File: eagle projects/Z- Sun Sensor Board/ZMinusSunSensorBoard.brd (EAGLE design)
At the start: 91 x 91 mm, 194 parts, among them J2 HIROSE_FH19C-6S-0.5SH(10), J3 HIROSE_FH19C-6S-0.5SH(10), J4 HIROSE_FH19C-6S-0.5SH(10), J5 HIROSE_FH19C-6S-0.5SH(10), U1 ADS7841E_2K5, U13 ADS7841E_2K5, U15 TLV9051IDCKR, U19 TLV9051IDCKR, U2 ADS7841E_2K5, U21 TLV9051IDCKR, U23 TLV9051IDCKR, U24 TLV9051IDCKR, U25 ADS7841E_2K5, U26 TLV9051IDCKR, U27 ADS7841E_2K5, U28 TLV9051IDCKR, U29 TLV9051IDCKR, U3 TLV9051IDCKR, U30 TLV9051IDCKR, U31 TLV9051IDCKR, U32 TLV9051IDCKR, U4 LM20BIM7X_NOPB, U6 TLV9051IDCKR, U8 TLV9051IDCKR, U9 TLV9051IDCKR

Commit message: Rev B almost ready
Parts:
- removed A1: XY_SUN_SENSOR, my_library:XY_SUN_SENOR_MASK
- removed C104, C107, C109, C112, C114, C31, C69, C86, C97: 0.1u, resistor:C0402
- removed C105, C110, C111, C115, C116, C33, C54, C70, C84, C98: 0.022u, resistor:C0402
- removed C106, C108, C113, C55, C68, C85, C99: 4.7u, resistor:C0402
- removed C30: 4.7u, rcl:C0805
- removed J4, J5: HIROSE_FH19C-6S-0.5SH(10), my_library:HIROSE_FH19C-6S-0.5SH(10)
- removed JP1: (no value), pinhead:1X02
- removed JP3: (no value), pinhead:2X05
- removed R2: 0R, rcl:R0805
- removed R28, R57, R63, R69: 13.7k, resistor:R0402
- removed R31, R46, R55, R61, R67: 3.74k, resistor:R0402
- removed R56, R62, R68: 280R, resistor:R0402
- removed TP12, TP18, TP20, TP7, TP8: TESTPOINT, my_library:TP_P76H50
- removed U15, U24, U28, U30, U31, U32: TLV9051IDCKR, my_library:SC70-5P65_210X110L36X22N_TLV9051
- added C10, C17, C24, C36, C39, C4, C58, C64, C7: 0.1u, resistor:C0402
- added C11, C18, C34, C37, C40, C5, C59, C8: 0.022u, resistor:C0402
- added C13, C23, C3, C35, C38, C44, C57, C6, C63, C9: 4.7u, rcl:C0805
- added C2: 0.1u, rcl:C0402
- added J1: TE-1734829-2, my_library:TE-1734829-2
- added JP2, JP4, JP5, JP6: (no value), my_library:1X06_MTG_HOLES
- added R27: 5.1M, rcl:R0402
- added R30, R37, R43, R49, R71, R79: 280R, resistor:R0402
- added R35, R41, R72, R74, R80: 13.7k, resistor:R0402
- added R36, R42, R73, R75, R81: 3.74k, resistor:R0402
- added TP23, TP24, TP25, TP27, TP29: TESTPOINT, my_library:TP_P76H50
- added U$1: SSR_MOUNT_03, my_library:SSR_MOUNT_03
- added U$3, U$4, U$5: (no value), my_library:PHOTODIODE_SILK
- added U10, U11, U12, U14, U16, U17: TSV991AILT, my_library:SOT95P280X145-5N
- added U5: LM20BIM7X_NOPB, my_library:SOT23-5P65_210X110L40X22N_LM20
- C100, C71: value 0.022u -> 4.7u; device resistor:C0402 -> rcl:C0805
- C101, C27, C32: value 0.022u -> 0.1u
- C103, C96: value 4.7u -> 0.022u
- C25, C28: value 4.7u -> 0.022u; device rcl:C0805 -> resistor:C0402
- C26, C29: value 0.1u -> 4.7u; device resistor:C0402 -> rcl:C0805
- C52, C82: value 4.7u -> 0.1u
- C53, C67, C83: value 0.1u -> 0.022u
- C87: device resistor:C0402 -> rcl:C0805
- J2: value HIROSE_FH19C-6S-0.5SH(10) -> (none); device my_library:HIROSE_FH19C-6S-0.5SH(10) -> my_library:2X05
- J3: value HIROSE_FH19C-6S-0.5SH(10) -> (none); device my_library:HIROSE_FH19C-6S-0.5SH(10) -> my_library:1X02
- LED1: device led:CHIP-LED0603 -> led:CHIPLED-0603-TTW
- R14, R25: value 280R -> 5.1M; device resistor:R0402 -> rcl:R0402
- R15: value 13.7k -> 5.1M; device resistor:R0402 -> rcl:R0402
- R17: device resistor:R0402 -> rcl:R0402
- R19: value 3.74k -> 5.1M; device resistor:R0402 -> rcl:R0402
- R44, R53, R59, R65: value 280R -> 13.7k
- R45, R54, R60, R66: value 13.7k -> 3.74k
- R58, R64, R70: value 3.74k -> 280R
- U19, U21, U23, U26, U29, U3, U6, U8, U9: value TLV9051IDCKR -> TSV991AILT; device my_library:SC70-5P65_210X110L36X22N_TLV9051 -> my_library:SOT95P280X145-5N
- moved R21 134.9 mm to (87.0, 73.0), flipped to the bottom
- moved R18 127.5 mm to (87.0, 67.9), flipped to the bottom
- moved R17 125.3 mm to (87.0, 70.5), flipped to the bottom
- moved R12 121.4 mm to (87.0, 74.3), flipped to the bottom
- moved R16 121.4 mm to (87.0, 69.2), flipped to the bottom
- moved J2 78.7 mm to (81.3, 69.2)
- moved C50 76.5 mm to (71.8, 88.6), turned to 180 degrees
- moved C49 75.0 mm to (71.8, 87.3), turned to 180 degrees
- moved J3 75.0 mm to (14.0, 71.4), turned to 180 degrees
- moved LED1 70.7 mm to (15.2, 75.6)
- moved R11 70.6 mm to (13.3, 75.6)
- moved C46 70.3 mm to (65.1, 87.3), turned to 180 degrees
- moved R60 69.2 mm to (77.5, 29.2), turned to 90 degrees
- moved U13 68.4 mm to (68.6, 83.8), turned to 180 degrees
- moved C45 68.4 mm to (61.9, 87.3), turned to 0 degrees
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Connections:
- removed net !CS!_SUN_Z+: U2.15
- removed net N$1: R2.1, U4.3
- removed net N$13: R14.2, R15.1, U9.1
- removed net N$3: A1.C1, C27.1, R7.1, U6.3
- removed net N$31: R22.2, R23.1, U3.1
- removed net N$34: R25.2, R28.1, U23.1
- removed net N$36: R32.2, R33.1, U24.1
- removed net N$45: R44.2, R45.1, U19.1
- removed net N$47: R50.2, R51.1, U21.1
- removed net N$48: LED1.A, R11.1
- removed net N$5: TP17.1, U25.2
- removed net N$56: R56.2, R57.1, U28.1
- removed net N$58: R59.2, R60.1, U29.1
- removed net N$64: R65.2, R66.1, U31.1
- removed net N$66: R68.2, R69.1, U32.1
- removed net N$68: JP3.10
- removed net N$9: R8.2, R9.1, U8.1
- removed net TEMP: R2.2, TP1.1, U2.2
- new net N$20: R27.1, U5.1
- new net N$21: LED1.A@1, R11.1
- new net N$27: C8.1, R13.1, U$1.C2, U8.4
- new net N$28: R8.2, R9.1, U8.3
- new net N$30: R43.2, R44.1, U12.3
- new net N$32: R22.2, R23.1, U3.3
- new net N$40: R30.2, R35.1, U9.3
- new net N$42: C18.1, R42.1, U$1.C1, U11.4
- new net N$43: R37.2, R41.1, U11.3
- new net N$60: R49.2, R53.1, U14.3
- new net N$69: R64.2, R65.1, U23.3
- new net N$71: R71.2, R72.1, U17.3
- new net N$74: R70.2, R74.1, U26.3
- new net N$78: R79.2, R80.1, U29.3
- new net TEMP_EXT: TP17.1, U25.2, U5.3
- new net TEMP_INT: TP1.1, U2.2, U4.3
- net !CS!_SUN_X+: now also J2.2; no longer JP3.2
- net !CS!_SUN_X-: now also J2.7; no longer JP3.7
- net !CS!_SUN_Y+: now also J2.4; no longer JP3.4
- net !CS!_SUN_Y-: now also J2.9; no longer JP3.9
- net !CS!_SUN_Z-: now also J2.6, U2.15; no longer JP3.6
- net +3V3: now also C10.1, C100.1, C101.1, C13.1, C17.1, C2.1, C23.1, C24.1, C27.1, C3.1, C32.1, C35.1, C36.1, C38.1, C39.1, C4.1, C44.1, C57.1, C58.1, C6.1, C63.1, C64.1, C7.1, C71.1, C9.1, J1.1, J2.10, J3.1, R35.2, R41.2, R44.2, R53.2, R59.2, R65.2, R72.2, R74.2, R80.2, U10.5, U11.5, U12.5, U14.5, U16.5, U17.5, U5.4; no longer C103.1, C104.1, C106.1, C107.1, C108.1, C109.1, C112.1, C113.1, C114.1, C25.1, C28.1, C30.1, C31.1, C53.1, C55.1, C67.1, C68.1, C69.1, C83.1, C85.1, C86.1, C96.1, C97.1, C99.1, JP1.1, R15.2, R28.2, R45.2, R54.2, R57.2, R60.2, R63.2, R66.2, R69.2, U15.5, U24.5, U28.5, U30.5, U31.5, U32.5
- net 0_DEGREES: now also C18.2, R42.2, TP24.1, U11.1; no longer C27.2, R7.2, TP3.1, U6.4
- net 120_DEGREES: now also C8.2, U8.1; no longer C32.2, U8.4
- net 240_DEGREES: now also C5.2, R7.2, TP3.1, U6.1; no longer C33.2, R19.2, TP8.1, U9.4
- net GND: now also C10.2, C100.2, C101.2, C13.2, C17.2, C2.2, C23.2, C24.2, C27.2, C3.2, C32.2, C35.2, C36.2, C38.2, C39.2, C4.2, C44.2, C57.2, C58.2, C6.2, C63.2, C64.2, C7.2, C71.2, C9.2, J1.2, JP2.2, JP2.4, JP2.6, JP4.2, JP4.4, JP4.6, JP5.2, JP5.4, JP5.6, JP6.2, JP6.4, JP6.6, LED1.C@1, R15.1, R19.1, R25.2, R27.2, R30.1, R37.1, R43.1, R49.1, R58.1, R64.1, R70.1, R71.1, R79.1, U$1.A1, U$1.A2, U$1.A3, U10.2, U11.2, U12.2, U14.2, U16.2, U17.2, U5.2, U5.5; no longer A1.A1, A1.A2, A1.A3, C103.2, C104.2, C106.2, C107.2, C108.2, C109.2, C112.2, C113.2, C114.2, C25.2, C28.2, C30.2, C31.2, C53.2, C55.2, C67.2, C68.2, C69.2, C83.2, C85.2, C86.2, C96.2, C97.2, C99.2, J2.2, J2.4, J2.6, J2.7, J2.8, J3.4, J3.6, J3.7, J3.8, J4.2, J4.4, J4.6, J4.7, J4.8, J5.2, J5.4, J5.6, J5.7, J5.8, JP1.2, LED1.C, R25.1, R44.1, R53.1, R56.1, R59.1, R62.1, R65.1, R68.1, U15.2, U24.2, U28.2, U30.2, U31.2, U32.2
- net N$10: now also R15.2
- net N$11: now also R14.2
- net N$12: now also C5.1, R7.1, U$1.C3, U6.4; no longer A1.C3, C33.1, R19.1, U9.3
- net N$14: now also R19.2
- net N$23: now also C96.1, JP6.3, R75.1, U26.4; no longer C100.1, J5.3, R31.1, U23.3
- net N$29: now also C83.1, JP6.1, R66.1, U23.4; no longer C84.1, J5.1, R24.1, U3.3
- net N$35: now also C103.1, JP6.5, R81.1, U29.4; no longer C101.1, J5.5, R34.1, U24.3
- net N$37: now also C34.1, JP5.1, R45.1, U12.4; no longer C98.1, J4.1, R64.1, U30.3
- net N$38: now also C25.1, JP4.1, U10.4; no longer C54.1, J3.1, U15.3
- net N$41: now also R32.2, R33.1, U16.3; no longer R38.2, R39.1, U15.1
- net N$44: now also C40.1, JP4.3, R24.1, U3.4; no longer C70.1, J3.3, R46.1, U19.3
- net N$46: now also C53.1, JP4.5, R34.1, U16.4; no longer C71.1, J3.5, R52.1, U21.3
- net N$49: now also C11.1, JP2.1, R36.1, U9.4; no longer C105.1, J2.1, R55.1, U26.3
- net N$54: now also R50.2, R51.1, U19.3; no longer R53.2, R54.1, U26.1
- net N$55: now also C28.1, JP2.3, R54.1, U14.4; no longer C110.1, J2.3, R58.1, U28.3
- net N$57: now also C37.1, JP2.5, R73.1, U17.4; no longer C111.1, J2.5, R61.1, U29.3
- net N$6: now also R38.2, R39.1, U10.3; no longer R1.2, R3.1, U6.1
- net N$61: now also R58.2, R59.1, U21.3; no longer R62.2, R63.1, U30.1
- net N$63: now also C59.1, JP5.3, R52.1, U19.4; no longer C115.1, J4.3, R67.1, U31.3
- net N$65: now also C67.1, JP5.5, R60.1, U21.4; no longer C116.1, J4.5, R70.1, U32.3
- net N$67: now also J2.8, R25.1; no longer JP3.8
- net N$8: now also R1.2, R3.1, U6.3; no longer A1.C2, C32.1, R13.1, U8.3
- net UCB0_SPI_CLK: now also J2.5; no longer JP3.5
- net UCB0_SPI_MISO: now also J2.1; no longer JP3.1
- net UCB0_SPI_MOSI: now also J2.3; no longer JP3.3
- net X+_0_DEGREES: now also C11.2, R36.2, U9.1; no longer C105.2, R55.2, U26.4
- net X+_120_DEGREES: now also C28.2, R54.2, TP16.1, U14.1; no longer C110.2, R58.2, TP15.1, U28.4
- net X+_240_DEGREES: now also C37.2, R73.2, TP25.1, U17.1; no longer C111.2, R61.2, TP16.1, U29.4
- net X-_0_DEGREES: now also C25.2, U10.1; no longer C54.2, U15.4
- net X-_120_DEGREES: now also C40.2, R24.2, TP5.1, U3.1; no longer C70.2, R46.2, TP11.1, U19.4
- net X-_240_DEGREES: now also C53.2, R34.2, TP9.1, U16.1; no longer C71.2, R52.2, TP12.1, U21.4
- net Y+_0_DEGREES: now also C34.2, R45.2, TP11.1, U12.1; no longer C98.2, R64.2, TP18.1, U30.4
- net Y+_120_DEGREES: now also C59.2, R52.2, TP15.1, U19.1; no longer C115.2, R67.2, TP19.1, U31.4
- net Y+_240_DEGREES: now also C67.2, R60.2, TP19.1, U21.1; no longer C116.2, R70.2, TP20.1, U32.4
- net Y-_0_DEGREES: now also C103.2, R81.2, TP29.1, U29.1; no longer C84.2, R24.2, TP5.1, U3.4
- net Y-_120_DEGREES: now also C96.2, R75.2, TP27.1, U26.1; no longer C100.2, R31.2, TP7.1, U23.4
- net Y-_240_DEGREES: now also C83.2, R66.2, TP23.1, U23.1; no longer C101.2, R34.2, TP9.1, U24.4
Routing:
- net +3V3: track 149.7 -> 488.3 mm, vias 42 -> 53
- net UCB0_SPI_CLK: track 6.65 -> 67.4 mm, vias 4 -> 0
- net UCB0_SPI_MISO: track 1.89 -> 60.6 mm, vias 1 -> 9
- net TEMP_EXT: track 0.00 -> 40.7 mm, vias 0 -> 1
- net N$3: track 35.5 -> 0.00 mm
- net N$52: track 0.00 -> 27.5 mm, vias 0 -> 2
- net !CS!_SUN_Y+: track 0.00 -> 26.0 mm, vias 0 -> 2
- net TEMP: track 21.9 -> 0.00 mm
- net N$50: track 0.00 -> 21.4 mm, vias 0 -> 2
- net N$51: track 0.00 -> 21.4 mm, vias 0 -> 2
- net N$14: track 2.34 -> 23.2 mm, vias 0 -> 4
- net TEMP_INT: track 0.00 -> 20.1 mm
- net N$27: track 0.00 -> 18.0 mm, vias 1 -> 0
- net 0_DEGREES: track 28.5 -> 45.9 mm
- net 240_DEGREES: track 22.2 -> 39.4 mm
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- added copper zone on layer 15, net +3V10
- added copper zone on layer 15, net +3V11
- added copper zone on layer 15, net +3V12
- added copper zone on layer 15, net +3V14
- added copper zone on layer 15, net +3V16
- added copper zone on layer 15, net +3V18
- added copper zone on layer 15, net +3V20
- added copper zone on layer 15, net +3V22
- added copper zone on layer 15, net +3V24
- added copper zone on layer 15, net +3V4
- added copper zone on layer 15, net +3V5
- added copper zone on layer 15, net +3V6
- added copper zone on layer 15, net +3V7
- added copper zone on layer 15, net +3V8
- added copper zone on layer 15, net +3V9
- added copper zone on layer 2, net GND10
- added copper zone on layer 2, net GND11
- added copper zone on layer 2, net GND13
- added copper zone on layer 2, net GND15
- added copper zone on layer 2, net GND17
- added copper zone on layer 2, net GND19
- added copper zone on layer 2, net GND21
- added copper zone on layer 2, net GND23
- added copper zone on layer 2, net GND3
- added copper zone on layer 2, net GND4
- added copper zone on layer 2, net GND5
- added copper zone on layer 2, net GND6
- added copper zone on layer 2, net GND7
- added copper zone on layer 2, net GND8
- added copper zone on layer 2, net GND9
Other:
- outline, holes or cut-outs redrawn
- board text removed: "U15"
- board text removed: "U19"
- board text removed: "U21"
- board text removed: "U23"
- board text removed: "U24"
- board text removed: "U26"
- board text removed: "U28"
- board text removed: "U29"
- board text removed: "U30"
- board text removed: "U31"
- board text removed: "U32"
- board text removed: "U6"
- board text removed: "U8"
- board text removed: "U9"

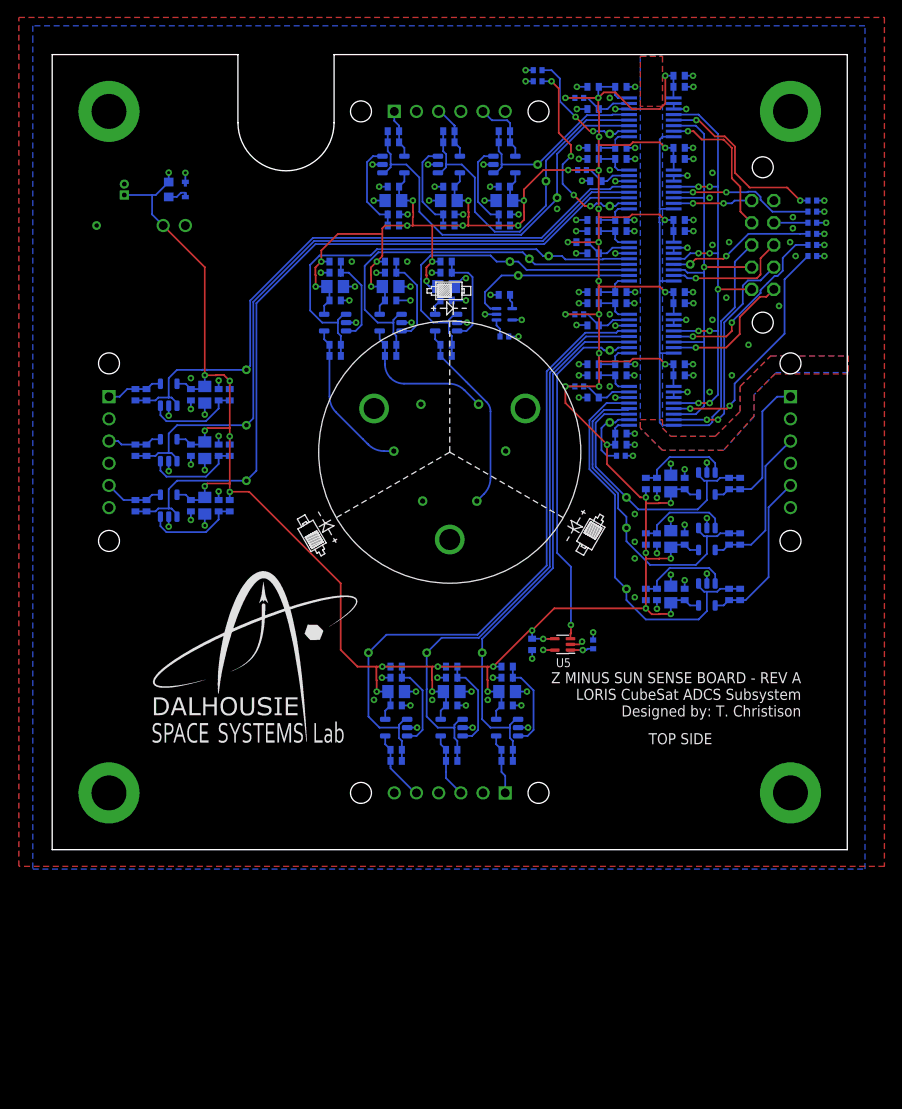
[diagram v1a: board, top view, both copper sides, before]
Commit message: Added cut to sun sense board for magnetorquer passthru
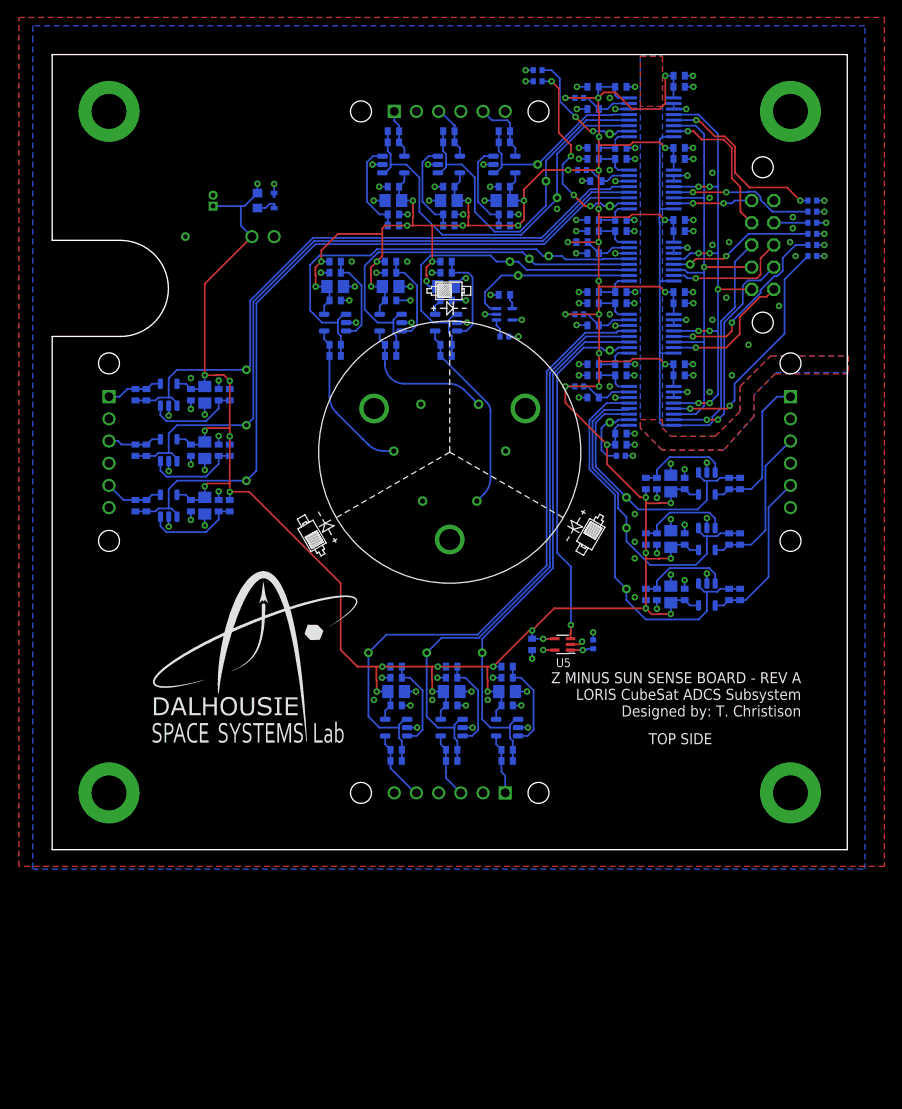
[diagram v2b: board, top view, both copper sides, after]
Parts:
- moved J1 10.2 mm to (18.4, 73.7)
- moved R11 10.2 mm to (23.5, 74.3)
- moved TP4 10.2 mm to (15.2, 70.2)
- moved J3 10.2 mm to (24.1, 70.2)
- moved LED1 10.2 mm to (25.4, 74.3)
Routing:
- net +3V3: track 488.3 -> 487.3 mm
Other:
- outline, holes or cut-outs redrawn
